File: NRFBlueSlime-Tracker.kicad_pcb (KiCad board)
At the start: 4 copper layers, 16.8 x 32.5 mm, 41 parts, among them J1 USB_C_Receptacle_USB2.0_16P, J2 Conn_01x05, J3 532610271, Q1 AO3401A, SW1 TS-1088-AR02016, U1 ANNA-B402-00B, U2 ICM-42688-P, U3 LIS2MDL, U4 ME6211C33R5G, U5 TP4057, X1 S2D32.768KB20F30T

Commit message: nrf52832 rev
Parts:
- removed C12: 10u, Capacitor_SMD:C_0402_1005Metric
- removed C13: 100n, Capacitor_SMD:C_0402_1005Metric
- removed D1: 1N5819WS, Diode_SMD:D_SOD-323
- removed D2: PRTR5V0U2X, Package_TO_SOT_SMD:SOT-143
- removed J3: 532610271, Connector_Molex:Molex_PicoBlade_53261-0271_1x02-1MP_P1.25mm_Horizontal
- removed LED2: NCD0402G1, LED_SMD:LED_0402_1005Metric
- removed LED3: NCD0402B1, LED_SMD:LED_0402_1005Metric
- removed Q1: AO3401A, Package_TO_SOT_SMD:SOT-23
- removed R10: 100k, Resistor_SMD:R_0402_1005Metric
- removed R11: 51k, Resistor_SMD:R_0402_1005Metric
- removed R12, R9: 10k, Resistor_SMD:R_0402_1005Metric
- C1: value 1u -> 10u
- C10, C11: value 10u -> 100n
- C7: value 100n -> 10u
- C9: value 10u -> 1u
- J1: value USB_C_Receptacle_USB2.0_16P -> 532610271; footprint Connector_USB:USB_C_Receptacle_G-Switch_GT-USB-7010ASV -> Connector_Molex:Molex_PicoBlade_53261-0271_1x02-1MP_P1.25mm_Horizontal
- J2: value Conn_01x05 -> Conn_01x06_Pin; footprint Connector_PinHeader_2.54mm:PinHeader_1x05_P2.54mm_Vertical -> Connector_PinHeader_2.54mm:PinHeader_1x06_P2.54mm_Vertical
- LED1: value NCD0402R1 -> NCD0402B1
- R1: value 5.1k -> 10k
- R2: value 5.1k -> 470
- R3: value 2.2k -> 100k
- R4: value 2.2k -> 1M
- R5: value 10k -> 2.2k
- R7: value 4.7k -> 10k
- R8: value 220 -> 51k
- U1: value ANNA-B402-00B -> ISP1507-AX-ST; footprint b402:ANNA-B402_UBL -> ISP1507-AX-ST:ISP1507AXST
- U5: value TP4057 -> SRV05-4; footprint nrfslime:SOT-23-6_L2.9-W1.6-P0.95-LS2.8-BL -> Package_TO_SOT_SMD:SOT-23-6
- moved U1 59.5 mm to (139.7, 88.8)
- moved C10 58.1 mm to (145.2, 86.1), turned to 90 degrees
- moved C2 56.8 mm to (139.8, 82.5), turned to 180 degrees
- moved C9 56.6 mm to (145.2, 88.0)
- moved C1 55.4 mm to (137.9, 82.5)
- moved R4 54.3 mm to (139.4, 76.5), turned to 0 degrees
- moved X1 53.0 mm to (142.4, 81.5), turned to 90 degrees
- moved U2 52.8 mm to (138.8, 80.5)
- moved C8 52.3 mm to (144.8, 81.3)
- moved C3 47.5 mm to (133.9, 80.4), turned to -90 degrees
- moved C4 46.6 mm to (134.9, 80.4), turned to -90 degrees
- moved C5 45.1 mm to (132.3, 82.4)
- moved U3 45.1 mm to (132.1, 80.6)
- moved U5 44.2 mm to (142.4, 65.5), turned to 90 degrees
- moved R1 43.0 mm to (132.0, 65.5)
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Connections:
- C11 pad 1: VDC -> Net-(C11-Pad1)
- C6 pad 1: +3V3 -> +BATT
- C8 pad 1: VBUS -> +3V3
- C9 pad 1: +BATT -> +3V3
- J2 pad 1: +3V3 -> +BATT
- J2 pad 4: GND -> RST
- J2 pad 5: RST -> GND
- LED1 pad 1: Net-(LED1-K) -> LED
- R1 pad 1: Net-(J1-CC1) -> +3V3
- R1 pad 2: GND -> KEY
- R2 pad 1: Net-(J1-CC2) -> +3V3
- R2 pad 2: GND -> Net-(LED1-A)
- R3 pad 1: +3V3 -> +BATT
- R3 pad 2: SCL -> BATLVL
- R4 pad 2: SDA -> DOCK
- R5 pad 2: RST -> SCL
- R6 pad 1: Net-(U5-PROG) -> +3V3
- R6 pad 2: GND -> SDA
- R7 pad 1: VBUS -> +3V3
- R7 pad 2: Net-(LED1-A) -> RST
- R8 pad 1: +3V3 -> BATLVL
- R8 pad 2: Net-(LED3-A) -> ADC_EN
- SW1 pad 2: Net-(C13-Pad1) -> Net-(C11-Pad1)
- U1 pad 1: unconnected-(U1-ANT_PCB-Pad1) -> GND
- U1 pad 10: unconnected-(U1-GPIO_10-Pad10) -> GND
- U1 pad 12: RST -> GND
- U1 pad 13: unconnected-(U1-GPIO_13-Pad13) -> RST
- U1 pad 14: /INT -> GND
- U1 pad 16: unconnected-(U1-SWO/GPIO_16-Pad16) -> GND
- U1 pad 17: /CLK -> unconnected-(U1-P0_22-Pad17)
- U1 pad 19: BATLVL -> unconnected-(U1-P0_24-Pad19)
- U1 pad 20: unconnected-(U1-GPIO_20-Pad20) -> Net-(U1-OUT_ANT)
- U1 pad 21: VBUS -> GND
- U1 pad 22: unconnected-(U1-NFC1/GPIO_22-Pad22) -> Net-(U1-OUT_ANT)
- U1 pad 23: unconnected-(U1-NFC2/GPIO_23-Pad23) -> GND
- U1 pad 24: unconnected-(U1-GPIO_24-Pad24) -> GND
- U1 pad 25: unconnected-(U1-GPIO_25-Pad25) -> GND
- U1 pad 26: unconnected-(U1-GPIO_26-Pad26) -> +3V3
- U1 pad 28: unconnected-(U1-GPIO_28-Pad28) -> SWD
- U1 pad 30: unconnected-(U1-GPIO_30-Pad30) -> SWC
- U1 pad 31: unconnected-(U1-GPIO_31-Pad31) -> GND
- U1 pad 32: unconnected-(U1-GPIO_32-Pad32) -> DOCK
- U1 pad 34: DP -> unconnected-(U1-P0_06-Pad34)
- U1 pad 35: DN -> unconnected-(U1-P0_04/AIN2-Pad35)
- U1 pad 36: LED -> unconnected-(U1-P0_05/AIN3-Pad36)
- U1 pad 37: KEY -> unconnected-(U1-P0_15/TRACE_DATA2-Pad37)
- U1 pad 38: SDA -> BATLVL
- U1 pad 39: SCL -> unconnected-(U1-P0_27-Pad39)
- U1 pad 4: GND -> unconnected-(U1-P0_10/NFC2-Pad4)
- U1 pad 40: unconnected-(U1-GPIO_40-Pad40) -> ADC_EN
- U1 pad 41: SWC -> LED
- U1 pad 42: SWD -> unconnected-(U1-P0_31/AIN7-Pad42)
- U1 pad 43: GND -> INT
- U1 pad 44: GND -> unconnected-(U1-P0_30/AIN6-Pad44)
- U1 pad 45: GND -> SDA
- U1 pad 46: GND -> unconnected-(U1-P0_29/AIN5-Pad46)
- U1 pad 47: unconnected-(U1-GPIO_47-Pad47) -> SCL
- U1 pad 5: Net-(U1-ANT) -> unconnected-(U1-P0_14/TRACE_DATA3-Pad5)
- U1 pad 53: GND -> unconnected-(U1-NOT_CONNECTED_5-Pad53)
- U1 pad 54: GND -> unconnected-(U1-NOT_CONNECTED_6-Pad54)
- U1 pad 55: GND -> unconnected-(U1-NOT_CONNECTED_7-Pad55)
- U1 pad 56: GND -> unconnected-(U1-NOT_CONNECTED_8-Pad56)
- U1 pad 6: Net-(U1-ANT) -> unconnected-(U1-P0_26-Pad6)
- U1 pad 9: +3V3 -> unconnected-(U1-P0_16/TRACE_DATA1-Pad9)
- U2 pad 4: /INT -> INT
- U4 pad 1: VDC -> +BATT
- U4 pad 3: VDC -> +BATT
- U5 pad 1: Net-(LED1-K) -> SWD
- U5 pad 3: +BATT -> SWC
- U5 pad 4: VBUS -> RST
- U5 pad 5: Net-(LED2-K) -> +BATT
- U5 pad 6: Net-(U5-PROG) -> DOCK
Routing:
- net +3V3: track 26.8 -> 74.0 mm, vias 8 -> 7
- net VBUS: track 39.5 -> 0.00 mm, vias 2 -> 0
- net DOCK: track 0.00 -> 30.3 mm, vias 0 -> 2
- net +BATT: track 11.6 -> 41.8 mm, vias 2 -> 3
- net DN: track 28.3 -> 0.00 mm, vias 2 -> 0
- net DP: track 26.8 -> 0.00 mm, vias 4 -> 0
- net ADC_EN: track 0.00 -> 26.1 mm, vias 0 -> 4
- net LED: track 3.30 -> 28.2 mm, vias 0 -> 2
- net KEY: track 22.6 -> 1.84 mm, vias 2 -> 0
- net BATLVL: track 7.50 -> 27.0 mm
- net INT: track 0.00 -> 11.2 mm, vias 0 -> 2
- net unconnected-(U1-ANT_PCB-Pad1): track 9.50 -> 0.00 mm
- net /CLK: track 10.4 -> 1.74 mm, vias 2 -> 0
- net /INT: track 8.40 -> 0.00 mm, vias 2 -> 0
- net VDC: track 8.18 -> 0.00 mm
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- removed copper zone on In2.Cu, net +3V3
- removed copper zone on In1.Cu, net GND
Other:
- board size 16.8 x 32.5 mm -> 30 x 31.8 mm
- copper layers 4 -> 2

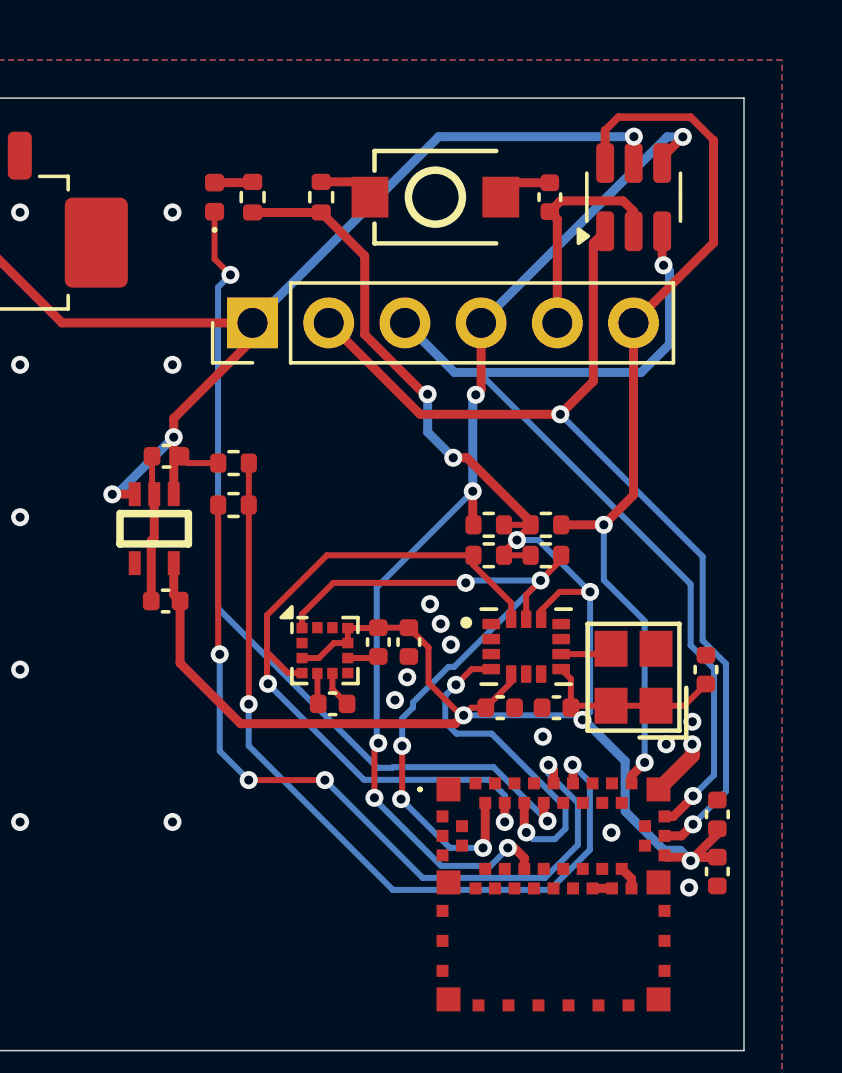
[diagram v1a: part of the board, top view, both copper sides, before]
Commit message: use metric spacing for dock, route switch
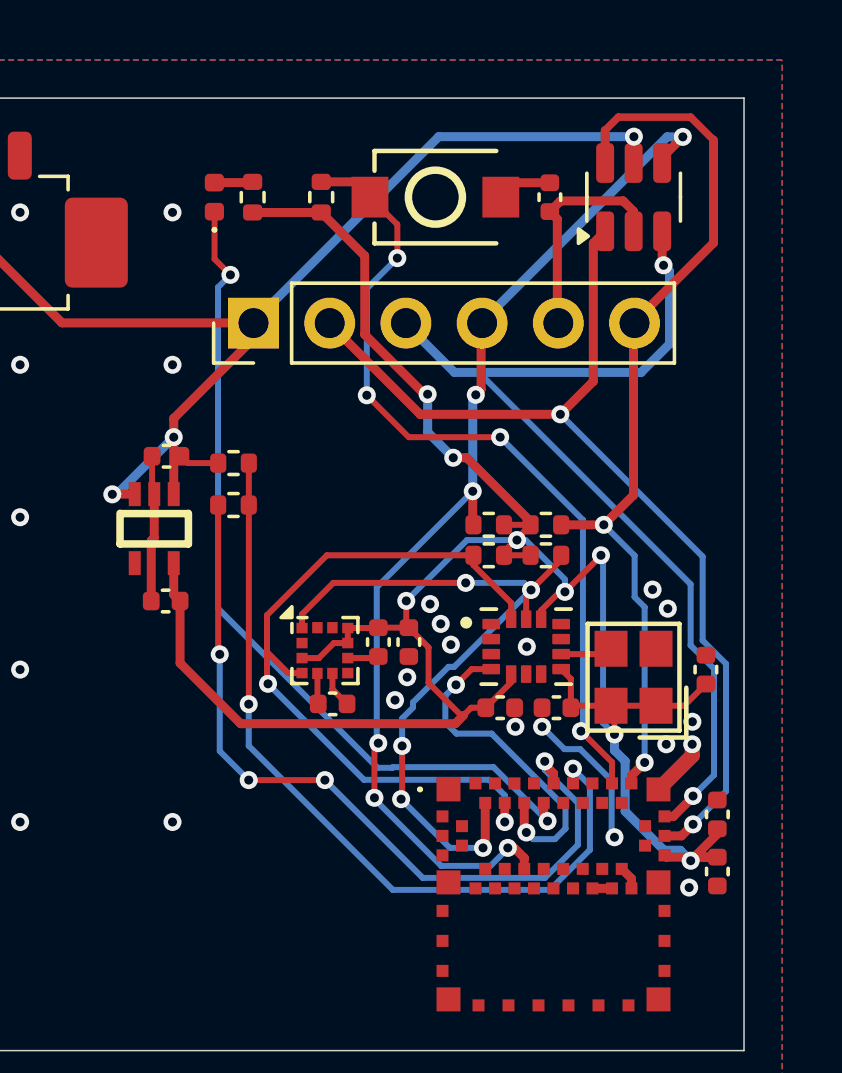
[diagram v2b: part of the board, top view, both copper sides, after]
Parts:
- R1: value 10k -> 100k
- R4: value 1M -> 100k
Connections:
- U1 pad 34: unconnected-(U1-P0_06-Pad34) -> KEY
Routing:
- net KEY: track 1.84 -> 27.4 mm, vias 0 -> 4
- net GND: track 17.5 -> 22.5 mm, vias 19 -> 23
- net +3V3: track 74.0 -> 76.9 mm, vias 7 -> 8
- net SCL: track 25.8 -> 25.0 mm

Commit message: mdbt42
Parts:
- added J3: Conn_01x01, TestPoint:TestPoint_Pad_4.0x4.0mm, B.Cu at (129.9, 95.5)
- added J4: Conn_01x01, TestPoint:TestPoint_Pad_4.0x4.0mm, B.Cu at (134.9, 95.5)
- added J5: Conn_01x01, TestPoint:TestPoint_Pad_4.0x4.0mm, B.Cu at (139.9, 95.5)
- added J6: Conn_01x01, TestPoint:TestPoint_Pad_4.0x4.0mm, B.Cu at (144.9, 95.5)
- added J7: Conn_01x01, TestPoint:TestPoint_Pad_4.0x4.0mm, B.Cu at (149.9, 95.5)
- J2: value Conn_01x06_Pin -> Conn_01x01; footprint Connector_PinHeader_2.54mm:PinHeader_1x06_P2.54mm_Vertical -> TestPoint:TestPoint_Pad_4.0x4.0mm; moved to B.Cu
- U1: value ISP1507-AX-ST -> MDBT42-512KV2; footprint ISP1507-AX-ST:ISP1507AXST -> MDBT42:MDBT42
- U4: value ME6211C33R5G -> RT9080-33GJ5; footprint nrfslime:SOT-353_L2.1-W1.3-P0.65-LS2.3-BL -> RT9080:TSOT-23-5_RIT
- moved U5 34.5 mm to (136.8, 99.5), turned to 0 degrees
- moved C6 29.5 mm to (146.2, 96.4), turned to 0 degrees
- moved R3 27.6 mm to (149.9, 92.4), turned to 90 degrees
- moved U4 26.6 mm to (146.7, 93.7), turned to 90 degrees
- moved J2 26.2 mm to (124.9, 95.5), turned to 180 degrees
- moved R8 26.2 mm to (150.4, 90.9), turned to 0 degrees
- moved C7 22.9 mm to (146.3, 91.0), turned to 0 degrees
- moved LED1 18.4 mm to (137.6, 81.5), turned to 180 degrees
- moved R4 17.5 mm to (148.7, 91.3), turned to -90 degrees
- moved C11 17.0 mm to (132.8, 81.1), turned to 90 degrees
- moved R2 16.8 mm to (137.6, 80.4), turned to 180 degrees
- moved U1 15.2 mm to (147.0, 75.5)
- moved R1 14.9 mm to (137.6, 79.3), turned to 180 degrees
- moved J1 14.0 mm to (127.2, 79.2)
- moved SW1 13.5 mm to (135.0, 79.0), turned to -90 degrees
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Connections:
- U1 pad 10: GND -> unconnected-(U1-P0.13-Pad10)
- U1 pad 12: GND -> unconnected-(U1-P0.10-Pad12)
- U1 pad 13: RST -> unconnected-(U1-P0.09-Pad13)
- U1 pad 15: unconnected-(U1-P0_20/TRACE_CLK-Pad15) -> +3V3
- U1 pad 16: GND -> DOCK
- U1 pad 17: unconnected-(U1-P0_22-Pad17) -> KEY
- U1 pad 18: GND -> unconnected-(U1-P0.07-Pad18)
- U1 pad 2: unconnected-(U1-P0_09/NFC1-Pad2) -> SCL
- U1 pad 20: Net-(U1-OUT_ANT) -> unconnected-(U1-P0.00/XL1-Pad20)
- U1 pad 21: GND -> unconnected-(U1-P0.01/XL2-Pad21)
- U1 pad 22: Net-(U1-OUT_ANT) -> unconnected-(U1-P0.04-Pad22)
- U1 pad 23: GND -> BATLVL
- U1 pad 24: GND -> ADC_EN
- U1 pad 26: +3V3 -> unconnected-(U1-DCC-Pad26)
- U1 pad 28: SWD -> unconnected-(U1-P0.31-Pad28)
- U1 pad 30: SWC -> LED
- U1 pad 31: GND -> unconnected-(U1-P0.30-Pad31)
- U1 pad 32: DOCK -> unconnected-(U1-P0.29-Pad32)
- U1 pad 34: KEY -> INT
- U1 pad 36: unconnected-(U1-P0_05/AIN3-Pad36) -> SDA
- U1 pad 37: unconnected-(U1-P0_15/TRACE_DATA2-Pad37) -> GND
- U1 pad 38: BATLVL -> unconnected-(U1-P0.24-Pad38)
- U1 pad 4: unconnected-(U1-P0_10/NFC2-Pad4) -> SWC
- U1 pad 40: ADC_EN -> unconnected-(U1-P0.16-Pad40)
- U1 pad 41: LED -> unconnected-(U1-P0.14-Pad41)
- U1 pad 5: unconnected-(U1-P0_14/TRACE_DATA3-Pad5) -> SWD
- U1 pad 6: unconnected-(U1-P0_26-Pad6) -> RST
- U1 pad 7: GND -> unconnected-(U1-P0.18-Pad7)
- U1 pad 8: GND -> unconnected-(U1-P0.17-Pad8)
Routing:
- net ADC_EN: track 26.5 -> 2.34 mm, vias 4 -> 0
- net BATLVL: track 26.8 -> 3.18 mm, vias 2 -> 0
- net +BATT: track 41.8 -> 59.9 mm, vias 3 -> 4
- net +3V3: track 76.9 -> 62.7 mm, vias 8 -> 5
- net LED: track 28.2 -> 14.7 mm
- net SDA: track 25.1 -> 34.7 mm, vias 2 -> 3
- net INT: track 11.2 -> 20.8 mm
- net KEY: track 27.4 -> 19.6 mm, vias 4 -> 2
- net GND: track 22.5 -> 16.7 mm, vias 23 -> 29
- net DOCK: track 30.3 -> 25.1 mm, vias 2 -> 3
- net SWD: track 33.3 -> 30.8 mm, vias 2 -> 4
- net RST: track 35.6 -> 33.2 mm, vias 6 -> 2
- net SWC: track 32.6 -> 33.7 mm
- net SCL: track 25.0 -> 24.2 mm, vias 5 -> 3
- net Net-(U1-OUT_ANT): track 0.65 -> 0.00 mm
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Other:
- board size 30 x 31.8 mm -> 30 x 26.8 mm
